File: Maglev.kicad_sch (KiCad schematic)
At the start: 25 parts, among them J1 629722000214, J2 691103110002, J3 61300621121, J4 61300821121, U1 WE-TVS-82400102, U2 ESP32-C3

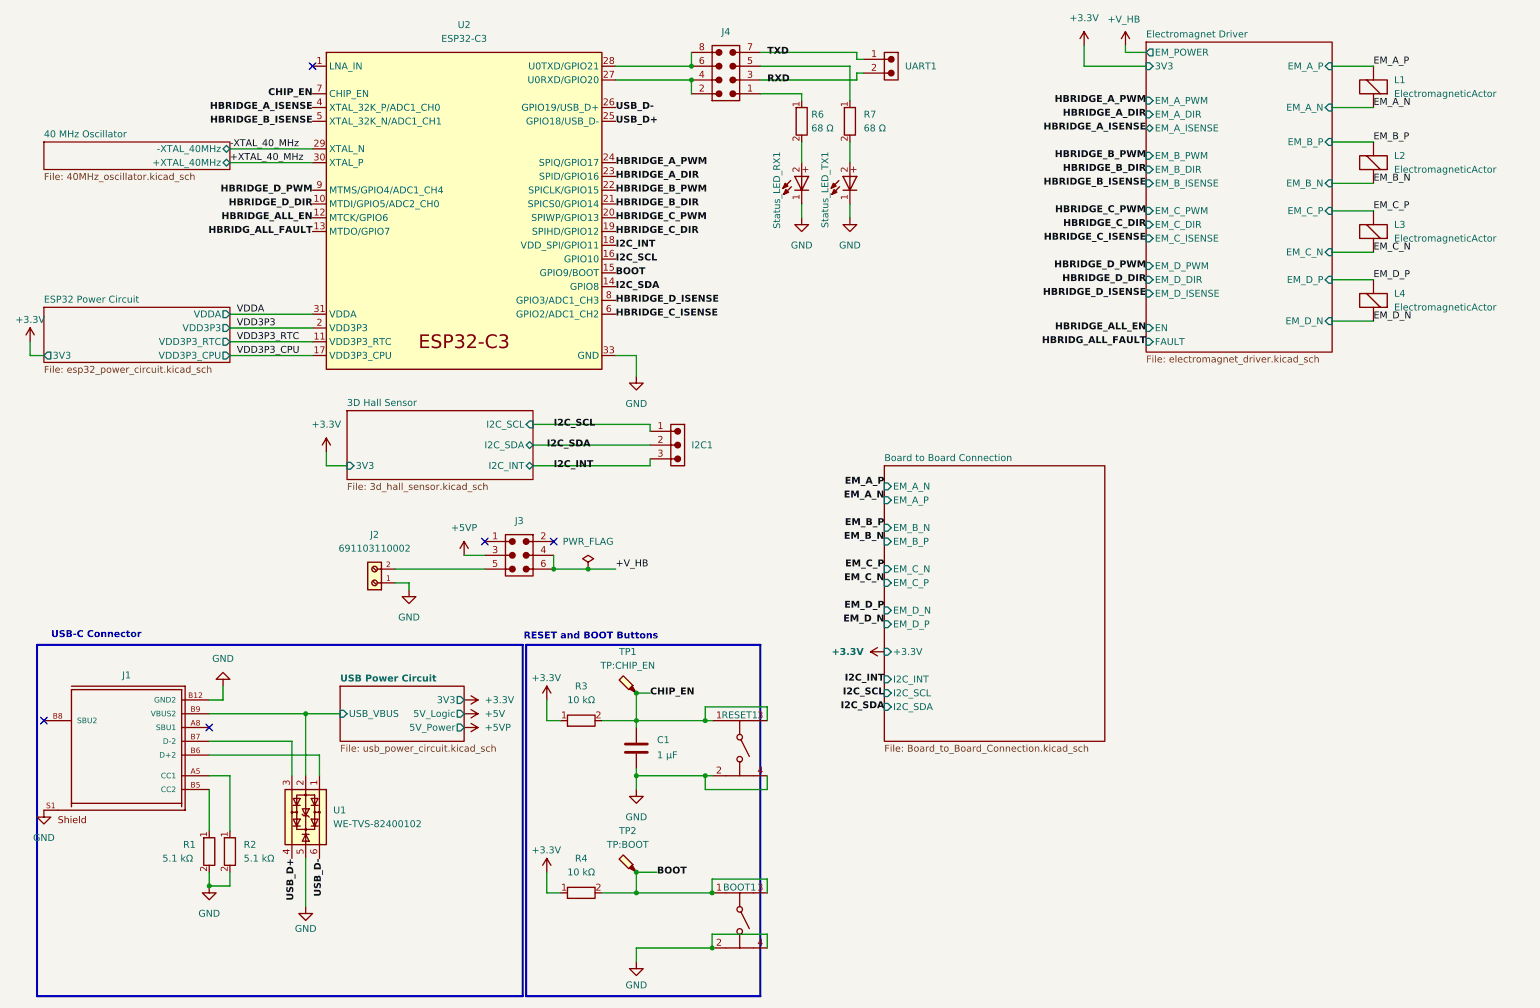
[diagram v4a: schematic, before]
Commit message: optimized quarz
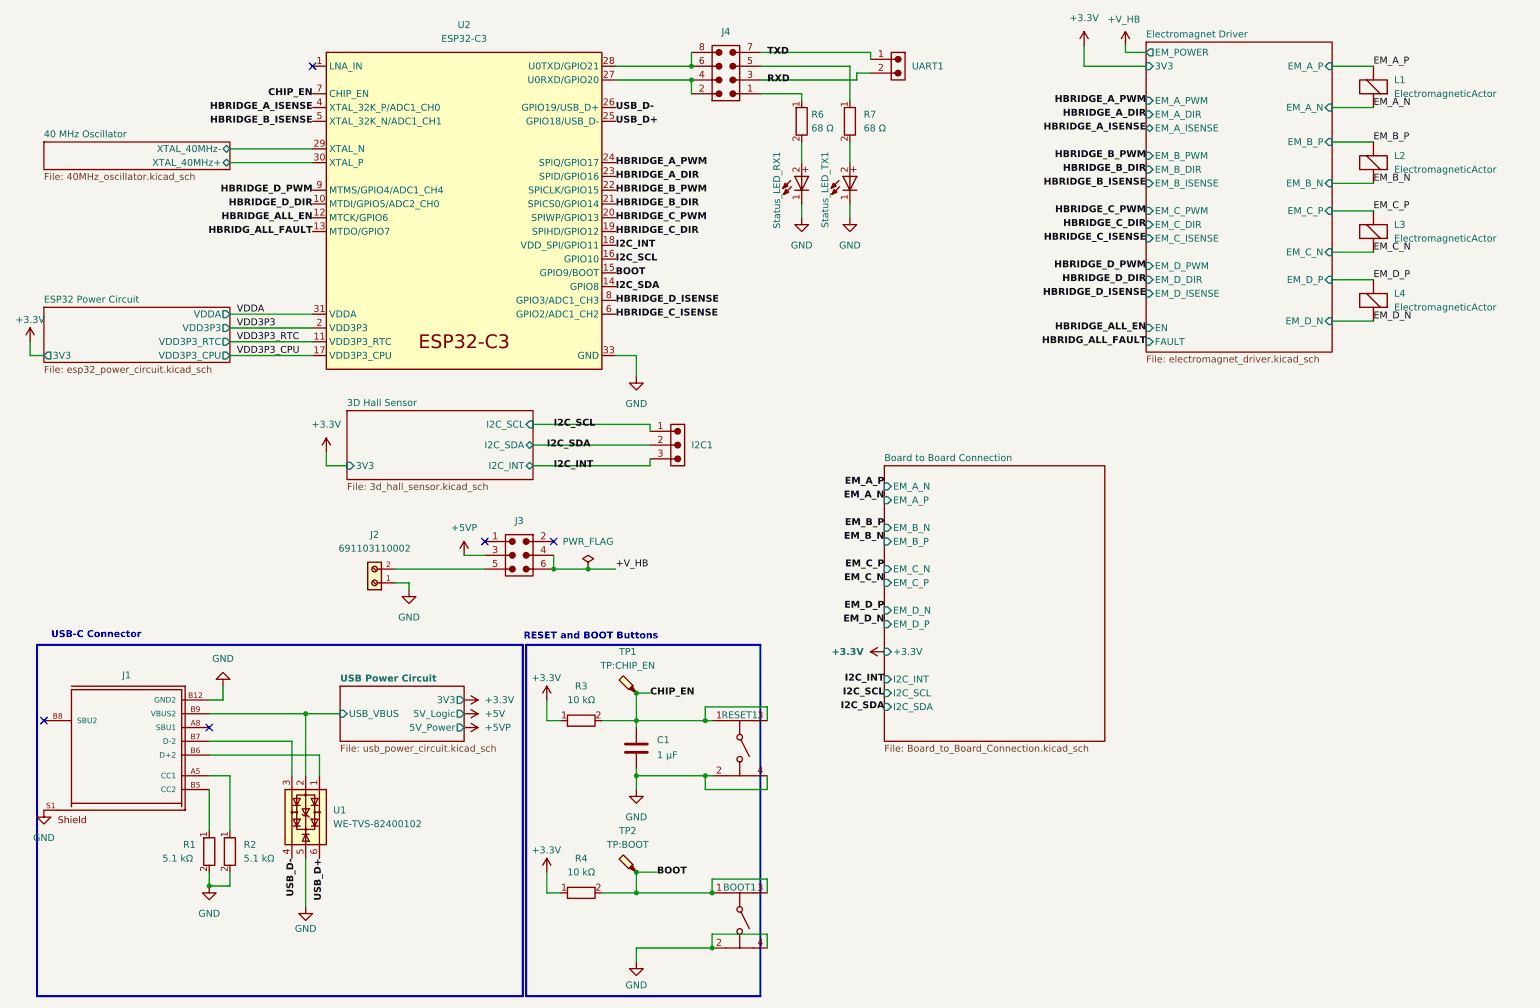
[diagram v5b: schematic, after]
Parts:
- U2: footprint PCM_Espressif:QFN-32-1EP_4x4mm_P0.4mm_EP2.9x2.9mm -> Package_DFN_QFN:QFN-32-1EP_5x5mm_P0.5mm_EP3.45x3.45mm
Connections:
- net USB_D+: now also U1.6; no longer U1.4
- net USB_D-: now also U1.4; no longer U1.6
- net +XTAL_40_MHz renamed 40 MHz Oscillator/XTAL_40MHz+
- net -XTAL_40_MHz renamed 40 MHz Oscillator/XTAL_40MHz-
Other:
- sheet 40 MHz Oscillator ports: added XTAL_40MHz+, XTAL_40MHz-; removed +XTAL_40MHz, -XTAL_40MHz
- moved on the sheet: UART1
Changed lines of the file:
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@@
 	(wire
 		(pts
+			(xy 49.53 41.91) (xy 64.77 41.91)
+		)
+		(stroke
+			(width 0)
+			(type default)
+		)
+	)
+	(wire
+		(pts
 			(xy 80.01 116.84) (xy 96.52 116.84)
 		)
@@
 	(wire
 		(pts
+			(xy 49.53 39.37) (xy 64.77 39.37)
+		)
+		(stroke
+			(width 0)
+			(type default)
+		)
+	)
+	(wire
+		(pts
 			(xy 134.62 21.59) (xy 134.62 24.13)
 		)
@@
 	(wire
 		(pts
+			(xy 165.1 26.67) (xy 165.1 25.4)
+		)
+		(stroke
+			(width 0)
+			(type default)
+		)
+	)
+	(wire
+		(pts
 			(xy 207.01 24.13) (xy 218.44 24.13)
 		)
@@
 	(wire
 		(pts
+			(xy 167.64 21.59) (xy 167.64 22.86)
+		)
+		(stroke
+			(width 0)
+			(type default)
+		)
+	)
+	(wire
+		(pts
 			(xy 148.59 184.15) (xy 148.59 186.69)
 		)
@@
 	(wire
 		(pts
-			(xy 12.7 77.47) (xy 15.24 77.47)
+			(xy 165.1 25.4) (xy 167.64 25.4)
 		)
 		(stroke
@@
 	(wire
 		(pts
-			(xy 124.46 153.67) (xy 124.46 154.94)
+			(xy 12.7 77.47) (xy 15.24 77.47)
 		)
 		(stroke
@@
 	(wire
 		(pts
-			(xy 165.1 26.67) (xy 165.1 25.4)
+			(xy 124.46 153.67) (xy 124.46 154.94)
 		)
 		(stroke
@@
 	(wire
 		(pts
-			(xy 166.37 22.86) (xy 165.1 22.86)
-		)
-		(stroke
-			(width 0)
-			(type default)
-		)
-	)
-	(wire
-		(pts
 			(xy 120.65 26.67) (xy 134.62 26.67)
 		)
@@
 	(wire
 		(pts
-			(xy 165.1 22.86) (xy 165.1 21.59)
-		)
-		(stroke
-			(width 0)
-			(type default)
-		)
-	)
-	(wire
-		(pts
 			(xy 45.72 140.97) (xy 48.26 140.97)
 		)
@@
 	(wire
 		(pts
-			(xy 166.37 25.4) (xy 165.1 25.4)
-		)
-		(stroke
-			(width 0)
-			(type default)
-		)
-	)
-	(wire
-		(pts
 			(xy 45.72 151.13) (xy 66.04 151.13)
 		)
@@
 	(wire
 		(pts
-			(xy 49.53 41.91) (xy 64.77 41.91)
-		)
-		(stroke
-			(width 0)
-			(type default)
-		)
-	)
-	(wire
-		(pts
 			(xy 118.11 144.78) (xy 124.46 144.78)
 		)
@@
 	(wire
 		(pts
-			(xy 147.32 21.59) (xy 165.1 21.59)
+			(xy 147.32 21.59) (xy 167.64 21.59)
 		)
 		(stroke
@@
 	(wire
 		(pts
-			(xy 49.53 39.37) (xy 64.77 39.37)
-		)
-		(stroke
-			(width 0)
-			(type default)
-		)
-	)
-	(wire
-		(pts
 			(xy 138.43 184.15) (xy 148.59 184.15)
 		)
@@
 		)
 	)
-	(label "-XTAL_40_MHz"
-		(at 49.53 39.37 0)
-		(effects
-			(font
-				(size 1.27 1.27)
-			)
-			(justify left bottom)
-		)
-	)
 	(label "I2C_SDA"
 		(at 107.95 93.98 0)
@@
 	)
 	(label "USB_D-"
-		(at 66.04 170.18 270)
+		(at 60.96 170.18 270)
 		(effects
 			(font
@@
 	)
 	(label "USB_D+"
-		(at 60.96 170.18 270)
+		(at 66.04 170.18 270)
 		(effects
 			(font
@@
 		)
 	)
-	(label "+XTAL_40_MHz"
-		(at 49.53 41.91 0)
-		(effects
-			(font
-				(size 1.27 1.27)
-			)
-			(justify left bottom)
-		)
-	)
 	(symbol
 		(lib_id "power:+5VP")
@@
 			)
 		)
-		(property "Footprint" "PCM_Espressif:QFN-32-1EP_4x4mm_P0.4mm_EP2.9x2.9mm"
+		(property "Footprint" "Package_DFN_QFN:QFN-32-1EP_5x5mm_P0.5mm_EP3.45x3.45mm"
 			(at 92.71 82.55 0)
 			(hide yes)
@@
 	(symbol
 		(lib_id "Connector_Wurth_WR-PHD:61300211121")
-		(at 171.45 24.13 270)
+		(at 172.72 24.13 270)
 		(unit 1)
 		(body_style 1)
@@
 		(fields_autoplaced yes)
 		(property "Reference" "UART1"
-			(at 173.99 24.1299 90)
+			(at 175.26 24.1299 90)
 			(show_name no)
 			(do_not_autoplace no)
@@
 		)
 		(property "Value" "61300211121"
-			(at 158.75 24.13 0)
+			(at 160.02 24.13 0)
 			(hide yes)
 			(show_name no)
@@
 		)
 		(property "Footprint" "Connector_THT_Wurth:J_Wurth_WR-PHD_61300211121"
-			(at 177.8 24.13 0)
+			(at 179.07 24.13 0)
 			(hide yes)
 			(show_name no)
@@
 		)
 		(property "Datasheet" "https://www.we-online.com/en/components/products/datasheet/61300211121?ki"
-			(at 184.15 64.77 0)
+			(at 185.42 64.77 0)
 			(hide yes)
 			(show_name no)
@@
 		)
 		(property "Description" "2.54 mm THT Pin Header"
-			(at 171.45 24.13 0)
+			(at 172.72 24.13 0)
 			(hide yes)
 			(show_name no)
@@
 		)
 		(property "Manufacturer" "Wurth Elektronik"
-			(at 181.61 64.77 0)
+			(at 182.88 64.77 0)
 			(hide yes)
 			(show_name no)
@@
 		)
 		(property "Manufacturer URL" "https://www.we-online.com"
-			(at 179.07 64.77 0)
+			(at 180.34 64.77 0)
 			(hide yes)
 			(show_name no)
@@
 		)
 		(property "Series" "WR-PHD"
-			(at 176.53 64.77 0)
+			(at 177.8 64.77 0)
 			(hide yes)
 			(show_name no)
@@
 		)
 		(property "Pitch" "2.54 mm"
-			(at 173.99 64.77 0)
+			(at 175.26 64.77 0)
 			(hide yes)
 			(show_name no)
@@
 		)
 		(property "Mounting Technology" "THT"
-			(at 171.45 64.77 0)
+			(at 172.72 64.77 0)
 			(hide yes)
 			(show_name no)
@@
 		)
 		(property "Pins (pcs)" "2"
-			(at 168.91 64.77 0)
+			(at 170.18 64.77 0)
 			(hide yes)
 			(show_name no)
@@
 		)
 		(property "Rows" "Single"
-			(at 166.37 64.77 0)
+			(at 167.64 64.77 0)
 			(hide yes)
 			(show_name no)
@@
 		)
 		(property "Gender" "Pin Header"
-			(at 163.83 64.77 0)
+			(at 165.1 64.77 0)
 			(hide yes)
 			(show_name no)
@@
 		)
 		(property "Type" "Straight"
-			(at 161.29 64.77 0)
+			(at 162.56 64.77 0)
 			(hide yes)
 			(show_name no)
@@
 		)
 		(property "IR (A)" "3"
-			(at 158.75 64.77 0)
+			(at 160.02 64.77 0)
 			(hide yes)
 			(show_name no)
@@
 			)
 		)
-		(pin "+XTAL_40MHz" bidirectional
+		(pin "XTAL_40MHz+" bidirectional
 			(at 49.53 41.91 0)
 			(effects
@@
 			)
 		)
-		(pin "-XTAL_40MHz" bidirectional
+		(pin "XTAL_40MHz-" bidirectional
 			(at 49.53 39.37 0)
 			(effects

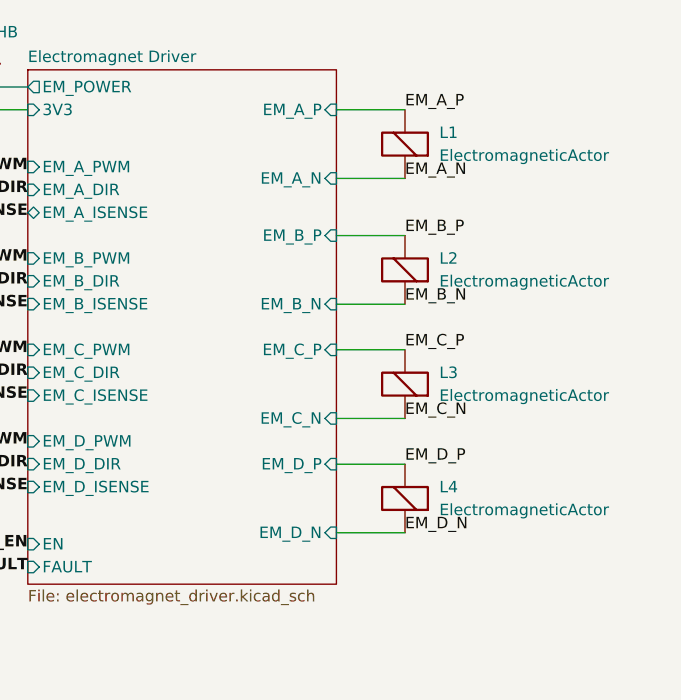
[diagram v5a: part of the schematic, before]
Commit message: more approvements regarding the manufacturer JLC
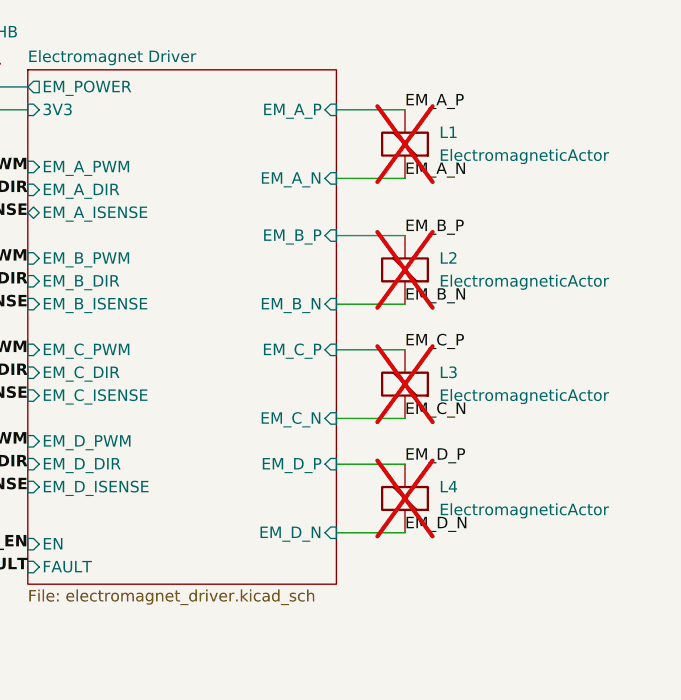
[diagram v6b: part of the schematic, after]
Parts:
- L1, L2, L3, L4: now not fitted
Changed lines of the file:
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@@
 		(on_board yes)
 		(in_pos_files yes)
-		(dnp no)
+		(dnp yes)
 		(fields_autoplaced yes)
 		(property "Reference" "L3"
@@
 		(on_board yes)
 		(in_pos_files yes)
-		(dnp no)
+		(dnp yes)
 		(fields_autoplaced yes)
 		(property "Reference" "L2"
@@
 		(on_board yes)
 		(in_pos_files yes)
-		(dnp no)
+		(dnp yes)
 		(fields_autoplaced yes)
 		(property "Reference" "L1"
@@
 		(on_board yes)
 		(in_pos_files yes)
-		(dnp no)
+		(dnp yes)
 		(fields_autoplaced yes)
 		(property "Reference" "L4"
